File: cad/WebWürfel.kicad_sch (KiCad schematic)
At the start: 41 parts, among them K1 1x03, T1 IRF9952, T2 FDN337N, T3 IRLML9301, U1 WeMos_D1_mini, U2 TSR1-2450

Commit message: old led grid
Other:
- company: (none) -> B.Braun Melsungen
- title: (none) -> D1 Web-Würfel
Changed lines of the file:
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@@
 (kicad_sch (version 20230121) (generator eeschema)
   (paper "A4")
+  (title_block
+    (title "D1 Web-Würfel")
+    (company "B.Braun Melsungen")
+  )
   (junction (at 26.035 64.135) (diameter 0) (color 0 0 0 0)
   )

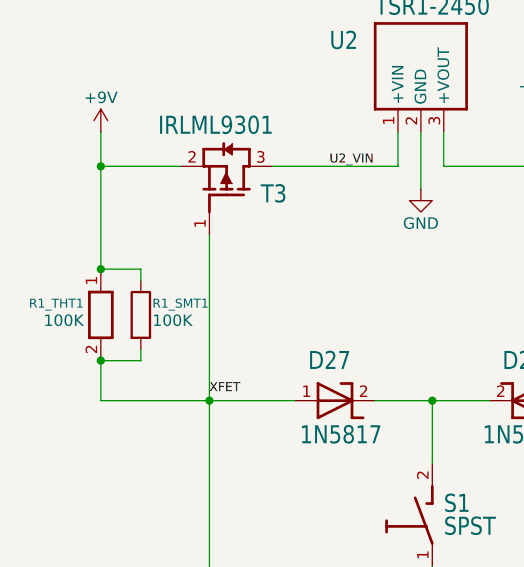
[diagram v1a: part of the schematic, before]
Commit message: rotated d1 mini by 90°
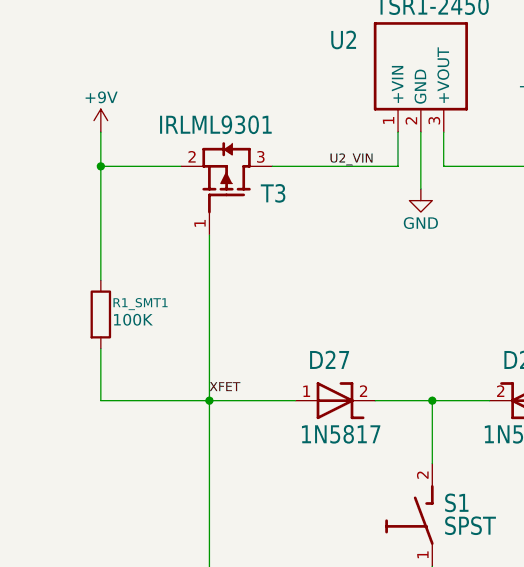
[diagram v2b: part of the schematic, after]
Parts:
- removed R1_THT1: 100K, D1Mini_Wuerfel_aktuell:0207_37, symbol D1Mini_Wuerfel_aktuell-eagle-import:R_KOHLE_1M_0207_37
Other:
- moved on the sheet: R1_SMT1

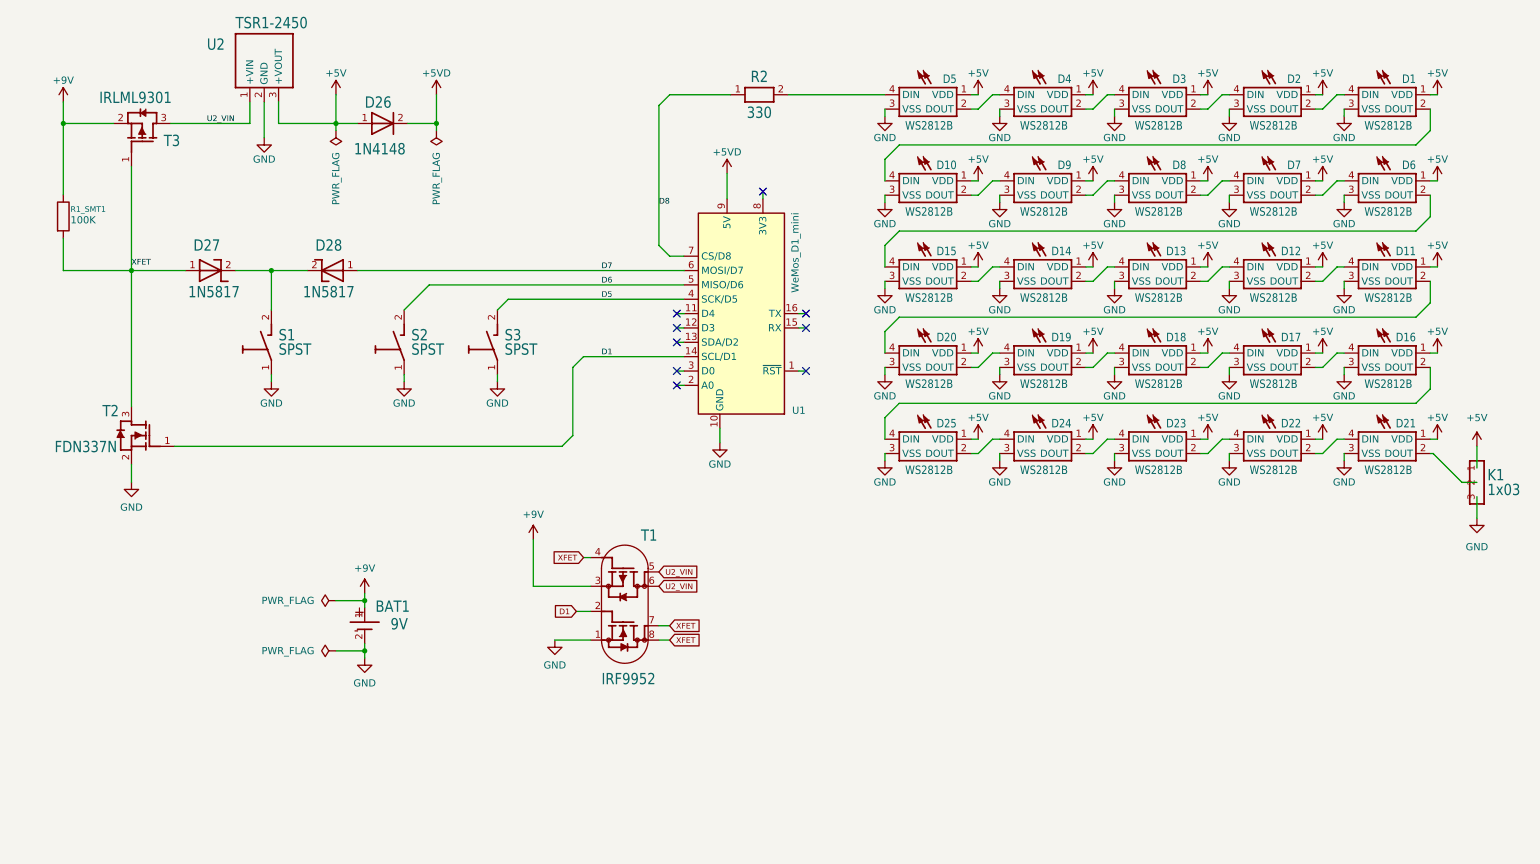
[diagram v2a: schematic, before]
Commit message: kicad update battery
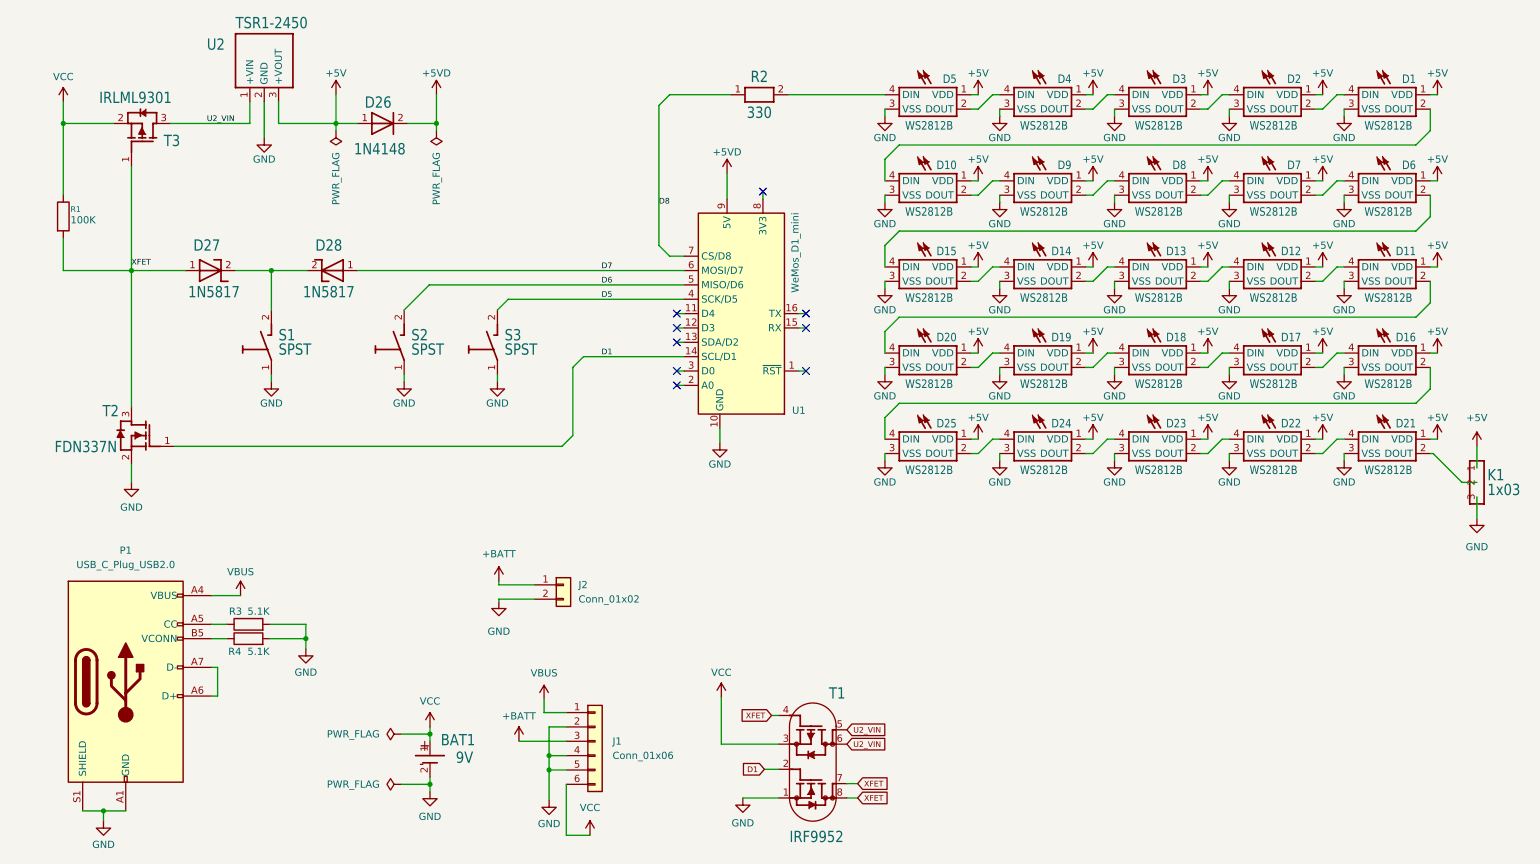
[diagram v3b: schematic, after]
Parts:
- added J1: Conn_01x06, Connector_PinHeader_2.54mm:PinHeader_1x06_P2.54mm_Vertical, symbol Connector_Generic:Conn_01x06
- added J2: Conn_01x02, Connector_JST:JST_PH_B2B-PH-K_1x02_P2.00mm_Vertical, symbol Connector_Generic:Conn_01x02
- added P1: USB_C_Plug_USB2.0, Connector_USB:USB_C_Receptacle_GCT_USB4085, symbol Connector:USB_C_Plug_USB2.0
- added R3, R4: 5.1K, Resistor_SMD:R_1206_3216Metric, symbol Device:R
- renumbered R1_SMT1 to R1
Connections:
- net GND: now also J1.2 (GND), J1.4 (GND), J1.5 (GND), J2.2 (Pin_2), P1.A1 (GND), P1.A12 (GND), P1.B1 (GND), P1.B12 (GND), P1.S1 (SHIELD), R3.2, R4.2
- net +9V renamed VCC
- net VCC: now also J1.6 (VOUT)
- new net: P1.A5 (CC), R3.1
- new net: P1.A6 (D+), P1.A7 (D-)
- new net: P1.B5 (VCONN), R4.1
- new net +BATT: J1.3 (BAT), J2.1 (Pin_1)
- new net VBUS: J1.1 (VIN), P1.A4 (VBUS), P1.A9 (VBUS), P1.B4 (VBUS), P1.B9 (VBUS)
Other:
- moved on the sheet: BAT1, T1
